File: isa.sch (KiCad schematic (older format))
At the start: 0 parts

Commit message: Began analog and digital schematic
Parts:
- added J?: Bus_ISA_8bit, symbol Bus_ISA_8bit
- added U?: 74LS245, symbol 74LS245
- added U?: 74LS688, symbol 74LS688
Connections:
- new net: J?.33 (DB7), U?.9 (A7)
- new net: J?.34 (DB6), U?.8 (A6)
- new net: J?.35 (DB5), U?.7 (A5)
- new net: J?.36 (DB4), U?.6 (A4)
- new net: J?.37 (DB3), U?.5 (A3)
- new net: J?.38 (DB2), U?.4 (A2)
- new net: J?.39 (DB1), U?.3 (A1)
- new net: J?.40 (DB0), U?.2 (A0)
- new net: J?.53 (BA09), U?.7 (R2)
- new net: J?.55 (BA07), U?.5 (R1)
- new net: J?.57 (BA05), U?.3 (R0)
- new net GND: U?.10 (GND), U?.10 (GND)
- new net VCC: U?.20 (VCC), U?.20 (VCC)
- no-connect marks 0 -> 11
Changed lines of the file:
@@
 $Descr A4 11693 8268
 encoding utf-8
-Sheet 1 3
+Sheet 1 1
 Title ""
 Date ""
@@
 Comment4 ""
 $EndDescr
+$Comp
+L Bus_ISA_8bit J?
+U 1 1 5B426BC4
+P 5500 3550
+F 0 "J?" H 5500 5225 50  0000 C CNN
+F 1 "Bus_ISA_8bit" H 5500 1875 50  0000 C CNN
+F 2 "" H 5500 3550 50  0001 C CNN
+F 3 "" H 5500 3550 50  0001 C CNN
+	1    5500 3550
+	1    0    0    -1
+$EndComp
+NoConn ~ 6400 3950
+NoConn ~ 6400 3850
+NoConn ~ 6400 3750
+NoConn ~ 6400 3650
+NoConn ~ 6400 3550
+NoConn ~ 6400 3450
+NoConn ~ 6400 3350
+NoConn ~ 6400 3250
+NoConn ~ 6400 3150
+NoConn ~ 6400 2050
+NoConn ~ 6400 4050
+$Comp
+L 74LS245 U?
+U 1 1 5B427009
+P 8250 2500
+F 0 "U?" H 8350 3075 50  0000 L BNN
+F 1 "74LS245" H 8300 1925 50  0000 L TNN
+F 2 "" H 8250 2500 50  0001 C CNN
+F 3 "" H 8250 2500 50  0001 C CNN
+	1    8250 2500
+	1    0    0    -1
+$EndComp
+Wire Wire Line
+	7550 2000 6400 2850
+Wire Wire Line
+	7550 2100 6400 2750
+Wire Wire Line
+	7550 2200 6400 2650
+Wire Wire Line
+	7550 2300 6400 2550
+Wire Wire Line
+	7550 2400 6400 2450
+Wire Wire Line
+	7550 2500 6400 2350
+Wire Wire Line
+	7550 2600 6400 2250
+Wire Wire Line
+	7550 2700 6400 2150
+$Comp
+L 74LS688 U?
+U 1 1 5B427266
+P 8300 4700
+F 0 "U?" H 8300 5650 50  0000 C CNN
+F 1 "74LS688" H 8300 3750 50  0000 C CNN
+F 2 "" H 8300 4700 50  0001 C CNN
+F 3 "" H 8300 4700 50  0001 C CNN
+	1    8300 4700
+	1    0    0    -1
+$EndComp
+Wire Wire Line
+	6400 4550 7600 4700
+Wire Wire Line
+	6400 4350 7600 4800
+Wire Wire Line
+	6400 4150 7600 4900
 $EndSCHEMATC

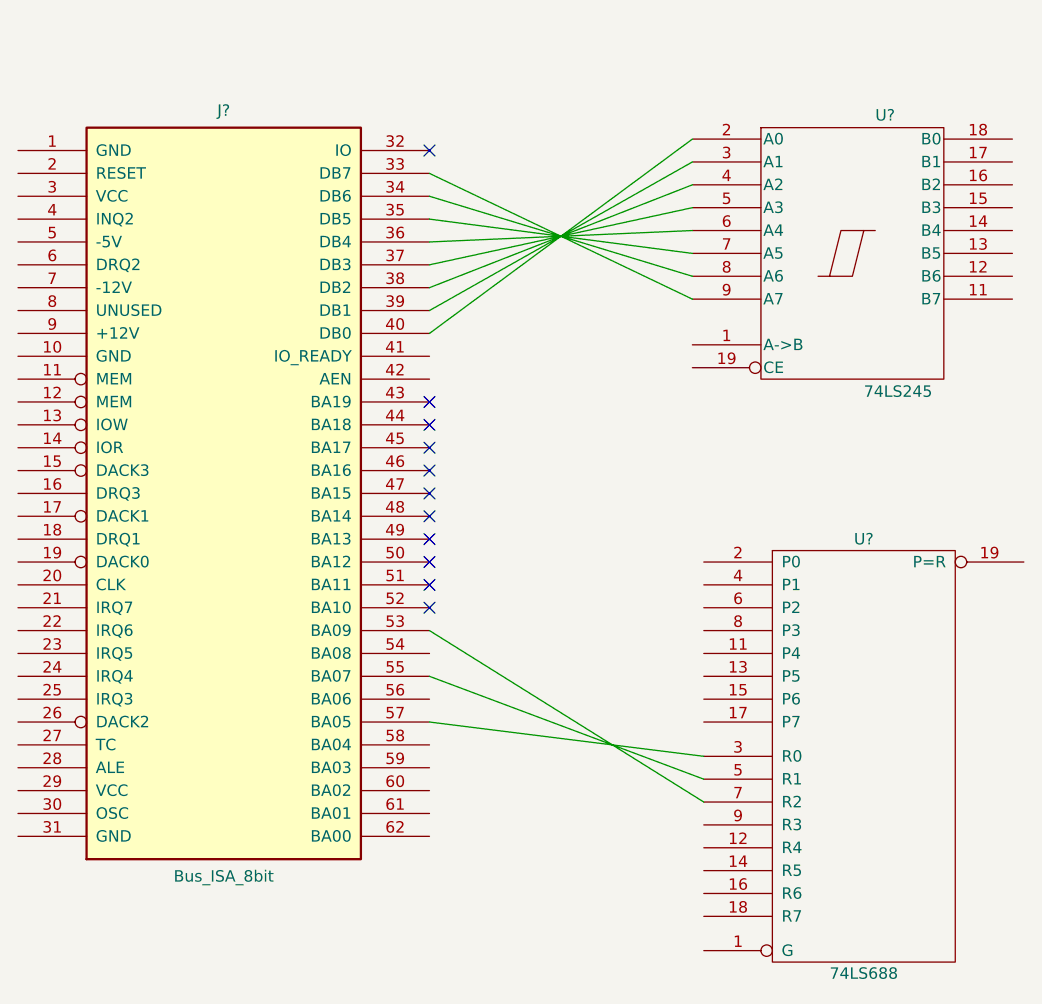
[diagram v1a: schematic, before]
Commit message: Fixed schematic to work with KiCad 5
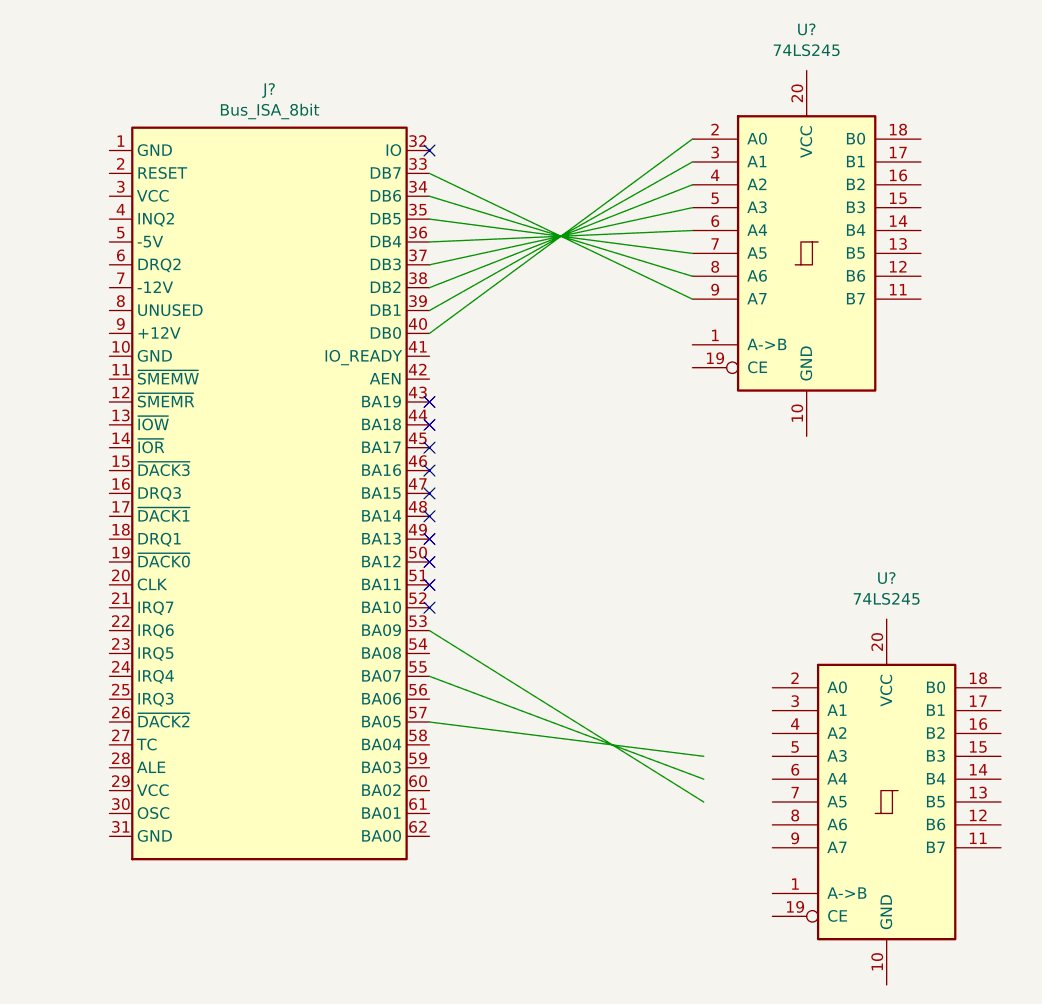
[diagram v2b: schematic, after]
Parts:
- removed J?: Bus_ISA_8bit, symbol Bus_ISA_8bit
- removed U?: 74LS245, symbol 74LS245
- removed U?: 74LS688, symbol 74LS688
- added J?: Bus_ISA_8bit, symbol Connector:Bus_ISA_8bit
- added U? (x2): 74LS245, symbol 74xx:74LS245
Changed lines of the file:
@@
-EESchema Schematic File Version 2
-LIBS:power
-LIBS:device
-LIBS:switches
-LIBS:relays
-LIBS:motors
-LIBS:transistors
-LIBS:conn
-LIBS:linear
-LIBS:regul
-LIBS:74xx
-LIBS:cmos4000
-LIBS:adc-dac
-LIBS:memory
-LIBS:xilinx
-LIBS:microcontrollers
-LIBS:dsp
-LIBS:microchip
-LIBS:analog_switches
-LIBS:motorola
-LIBS:texas
-LIBS:intel
-LIBS:audio
-LIBS:interface
-LIBS:digital-audio
-LIBS:philips
-LIBS:display
-LIBS:cypress
-LIBS:siliconi
-LIBS:opto
-LIBS:atmel
-LIBS:contrib
-LIBS:valves
-EELAYER 25 0
+EESchema Schematic File Version 4
+EELAYER 26 0
 EELAYER END
 $Descr A4 11693 8268
 encoding utf-8
-Sheet 1 1
+Sheet 2 5
 Title ""
 Date ""
@@
 Comment4 ""
 $EndDescr
-$Comp
-L Bus_ISA_8bit J?
-U 1 1 5B426BC4
-P 5500 3550
-F 0 "J?" H 5500 5225 50  0000 C CNN
-F 1 "Bus_ISA_8bit" H 5500 1875 50  0000 C CNN
-F 2 "" H 5500 3550 50  0001 C CNN
-F 3 "" H 5500 3550 50  0001 C CNN
-	1    5500 3550
-	1    0    0    -1
-$EndComp
 NoConn ~ 6400 3950
 NoConn ~ 6400 3850
@@
 NoConn ~ 6400 2050
 NoConn ~ 6400 4050
-$Comp
-L 74LS245 U?
-U 1 1 5B427009
-P 8250 2500
-F 0 "U?" H 8350 3075 50  0000 L BNN
-F 1 "74LS245" H 8300 1925 50  0000 L TNN
-F 2 "" H 8250 2500 50  0001 C CNN
-F 3 "" H 8250 2500 50  0001 C CNN
-	1    8250 2500
-	1    0    0    -1
-$EndComp
 Wire Wire Line
 	7550 2000 6400 2850
@@
 Wire Wire Line
 	7550 2700 6400 2150
-$Comp
-L 74LS688 U?
-U 1 1 5B427266
-P 8300 4700
-F 0 "U?" H 8300 5650 50  0000 C CNN
-F 1 "74LS688" H 8300 3750 50  0000 C CNN
-F 2 "" H 8300 4700 50  0001 C CNN
-F 3 "" H 8300 4700 50  0001 C CNN
-	1    8300 4700
-	1    0    0    -1
-$EndComp
 Wire Wire Line
 	6400 4550 7600 4700
@@
 Wire Wire Line
 	6400 4150 7600 4900
+$Comp
+L 74xx:74LS245 U?
+U 1 1 5BDFD7F3
+P 8050 2500
+F 0 "U?" H 8050 3478 50  0000 C CNN
+F 1 "74LS245" H 8050 3387 50  0000 C CNN
+F 2 "" H 8050 2500 50  0001 C CNN
+F 3 "http://www.ti.com/lit/gpn/sn74LS245" H 8050 2500 50  0001 C CNN
+	1    8050 2500
+	1    0    0    -1
+$EndComp
+$Comp
+L 74xx:74LS245 U?
+U 1 1 5BDFD9BF
+P 8400 4900
+F 0 "U?" H 8400 5878 50  0000 C CNN
+F 1 "74LS245" H 8400 5787 50  0000 C CNN
+F 2 "" H 8400 4900 50  0001 C CNN
+F 3 "http://www.ti.com/lit/gpn/sn74LS245" H 8400 4900 50  0001 C CNN
+	1    8400 4900
+	1    0    0    -1
+$EndComp
+$Comp
+L Connector:Bus_ISA_8bit J?
+U 1 1 5BDFDF92
+P 5700 3550
+F 0 "J?" H 5700 5317 50  0000 C CNN
+F 1 "Bus_ISA_8bit" H 5700 5226 50  0000 C CNN
+F 2 "" H 5700 3550 50  0001 C CNN
+F 3 "https://en.wikipedia.org/wiki/Industry_Standard_Architecture" H 5700 3550 50  0001 C CNN
+	1    5700 3550
+	1    0    0    -1
+$EndComp
 $EndSCHEMATC
